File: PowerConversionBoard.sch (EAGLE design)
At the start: 31 parts, among them U1 LM2678, U2 LM2678

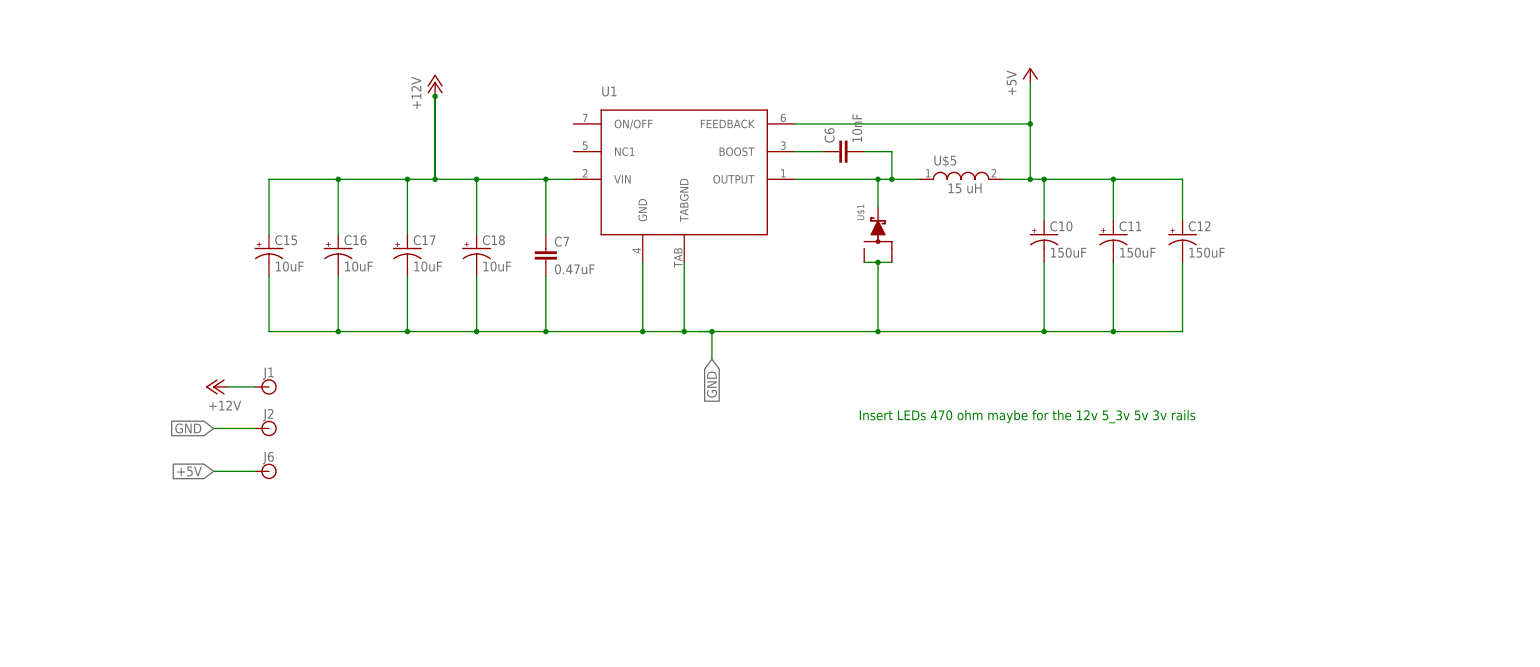
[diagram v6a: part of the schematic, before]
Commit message: Added LEDs to schematic
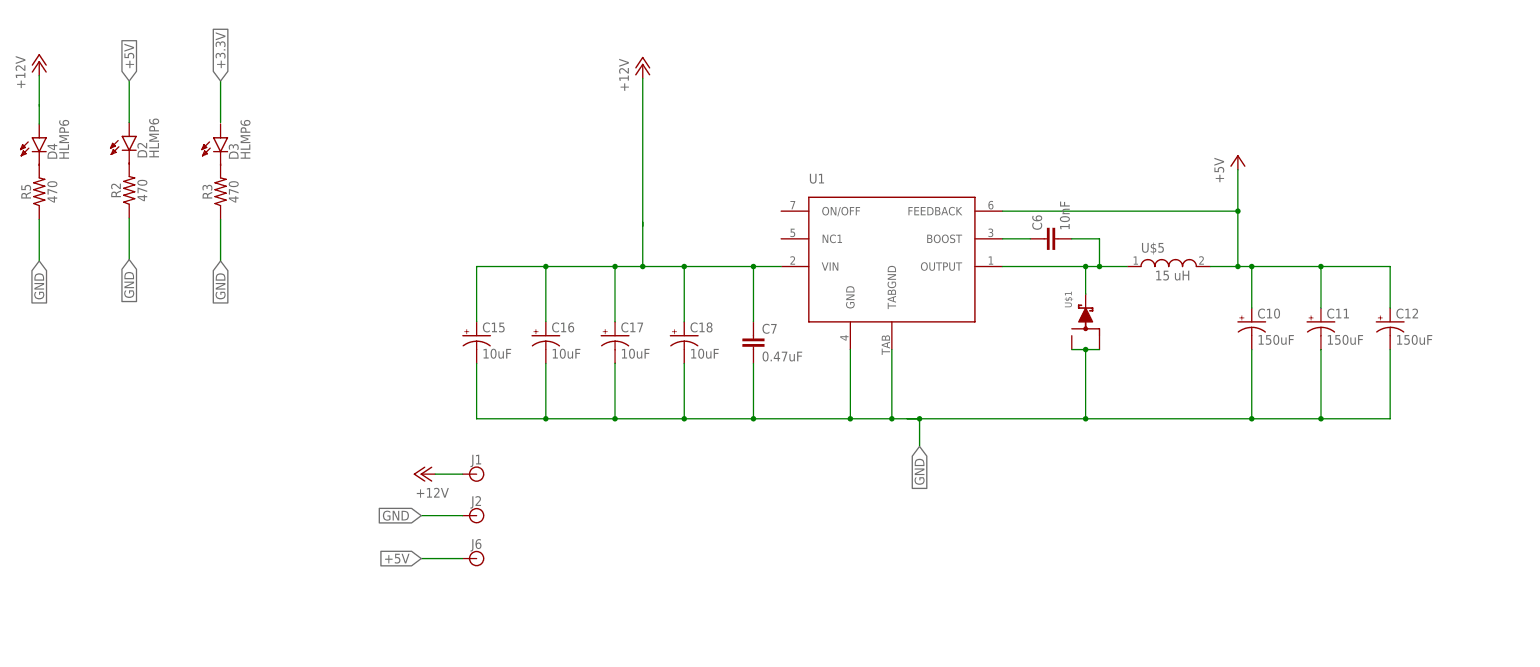
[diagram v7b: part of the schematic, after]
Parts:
- added D2, D3, D4: HLMP6, display-hp:HLMP6
- added R2, R3, R5: 470, SparkFun-Resistors:470OHM-0603-1/10W-1%
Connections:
- new net N$4: C15.+, C16.+, C17.+, C18.+, C7.1, U1.VIN
- net +12V: now also D4.A; no longer C15.+, C16.+, C17.+, C18.+, C7.1, U1.VIN
- net +5V: now also D2.A
- net GND: now also R2.1, R3.1, R5.1
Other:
- note removed: "Insert LEDs 470 ohm maybe for the 12v 5_3v 5v 3v rails"
- moved on the sheet: C10, C11, C12, C15, C16, C17, C18, C6, C7, J1, J2, J6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

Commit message: Put in good LEDs
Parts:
- removed D2, D3, D4: HLMP6, display-hp:HLMP6
- added LED1, LED2, LED3: (no value), led:LEDCHIP-LED0603
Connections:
- new net N$5: LED3.A, R3.1
- net +12V: now also R5.2; no longer D4.A
- net +3.3V: now also R3.2
- net +5V: now also R2.2; no longer D2.A
- net GND: now also LED1.C, LED2.C, LED3.C; no longer R2.1, R3.1, R5.1
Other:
- moved on the sheet: R2, R3, R5
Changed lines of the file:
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@@
 <part name="U$5" library="HCM1305" deviceset="HCM1305" device=""/>
 <part name="P+6" library="supply1" library_urn="urn:adsk.eagle:library:371" deviceset="+12V" device=""/>
+<part name="P+7" library="supply1" library_urn="urn:adsk.eagle:library:371" deviceset="+12V" device=""/>
+<part name="R5" library="SparkFun-Resistors" library_urn="urn:adsk.eagle:library:532" deviceset="470OHM" device="-0603-1/10W-1%" package3d_urn="urn:adsk.eagle:package:39650/1" value="470"/>
 <part name="R2" library="SparkFun-Resistors" library_urn="urn:adsk.eagle:library:532" deviceset="470OHM" device="-0603-1/10W-1%" package3d_urn="urn:adsk.eagle:package:39650/1" value="470"/>
-<part name="D2" library="display-hp" library_urn="urn:adsk.eagle:library:212" deviceset="HLMP6" device="" package3d_urn="urn:adsk.eagle:package:12992/1"/>
-<part name="R5" library="SparkFun-Resistors" library_urn="urn:adsk.eagle:library:532" deviceset="470OHM" device="-0603-1/10W-1%" package3d_urn="urn:adsk.eagle:package:39650/1" value="470"/>
-<part name="D4" library="display-hp" library_urn="urn:adsk.eagle:library:212" deviceset="HLMP6" device="" package3d_urn="urn:adsk.eagle:package:12992/1"/>
+<part name="LED1" library="led" library_urn="urn:adsk.eagle:library:259" deviceset="LED" device="CHIP-LED0603" package3d_urn="urn:adsk.eagle:package:15819/3"/>
+<part name="LED2" library="led" library_urn="urn:adsk.eagle:library:259" deviceset="LED" device="CHIP-LED0603" package3d_urn="urn:adsk.eagle:package:15819/3"/>
 <part name="R3" library="SparkFun-Resistors" library_urn="urn:adsk.eagle:library:532" deviceset="470OHM" device="-0603-1/10W-1%" package3d_urn="urn:adsk.eagle:package:39650/1" value="470"/>
-<part name="D3" library="display-hp" library_urn="urn:adsk.eagle:library:212" deviceset="HLMP6" device="" package3d_urn="urn:adsk.eagle:package:12992/1"/>
-<part name="P+7" library="supply1" library_urn="urn:adsk.eagle:library:371" deviceset="+12V" device=""/>
+<part name="LED3" library="led" library_urn="urn:adsk.eagle:library:259" deviceset="LED" device="CHIP-LED0603" package3d_urn="urn:adsk.eagle:package:15819/3"/>
 </parts>
 <sheets>
@@
 <attribute name="VALUE" x="-8.128" y="87.376" size="1.778" layer="96" rot="R90"/>
 </instance>
-<instance part="R2" gate="G$1" x="-99.822" y="69.342" smashed="yes" rot="R90">
-<attribute name="NAME" x="-101.346" y="69.342" size="1.778" layer="95" font="vector" rot="R90" align="bottom-center"/>
-<attribute name="VALUE" x="-98.298" y="69.342" size="1.778" layer="96" font="vector" rot="R90" align="top-center"/>
-</instance>
-<instance part="D2" gate="A" x="-99.822" y="76.708" smashed="yes">
-<attribute name="NAME" x="-96.52" y="75.184" size="1.778" layer="95" rot="R90"/>
-<attribute name="VALUE" x="-94.361" y="75.184" size="1.778" layer="96" rot="R90"/>
-</instance>
-<instance part="R5" gate="G$1" x="-116.332" y="69.088" smashed="yes" rot="R90">
-<attribute name="NAME" x="-117.856" y="69.088" size="1.778" layer="95" font="vector" rot="R90" align="bottom-center"/>
-<attribute name="VALUE" x="-114.808" y="69.088" size="1.778" layer="96" font="vector" rot="R90" align="top-center"/>
-</instance>
-<instance part="D4" gate="A" x="-116.332" y="76.454" smashed="yes">
-<attribute name="NAME" x="-113.03" y="74.93" size="1.778" layer="95" rot="R90"/>
-<attribute name="VALUE" x="-110.871" y="74.93" size="1.778" layer="96" rot="R90"/>
-</instance>
-<instance part="R3" gate="G$1" x="-83.058" y="69.088" smashed="yes" rot="R90">
-<attribute name="NAME" x="-84.582" y="69.088" size="1.778" layer="95" font="vector" rot="R90" align="bottom-center"/>
-<attribute name="VALUE" x="-81.534" y="69.088" size="1.778" layer="96" font="vector" rot="R90" align="top-center"/>
-</instance>
-<instance part="D3" gate="A" x="-83.058" y="76.454" smashed="yes">
-<attribute name="NAME" x="-79.756" y="74.93" size="1.778" layer="95" rot="R90"/>
-<attribute name="VALUE" x="-77.597" y="74.93" size="1.778" layer="96" rot="R90"/>
-</instance>
 <instance part="P+7" gate="1" x="-116.332" y="92.964" smashed="yes">
 <attribute name="VALUE" x="-118.872" y="87.884" size="1.778" layer="96" rot="R90"/>
+</instance>
+<instance part="R5" gate="G$1" x="-116.332" y="76.454" smashed="yes" rot="R90">
+<attribute name="NAME" x="-117.856" y="76.454" size="1.778" layer="95" font="vector" rot="R90" align="bottom-center"/>
+<attribute name="VALUE" x="-114.808" y="76.454" size="1.778" layer="96" font="vector" rot="R90" align="top-center"/>
+</instance>
+<instance part="R2" gate="G$1" x="-99.822" y="76.708" smashed="yes" rot="R90">
+<attribute name="NAME" x="-101.346" y="76.708" size="1.778" layer="95" font="vector" rot="R90" align="bottom-center"/>
+<attribute name="VALUE" x="-98.298" y="76.708" size="1.778" layer="96" font="vector" rot="R90" align="top-center"/>
+</instance>
+<instance part="LED1" gate="G$1" x="-116.332" y="69.088" smashed="yes">
+<attribute name="NAME" x="-112.776" y="64.516" size="1.778" layer="95" rot="R90"/>
+<attribute name="VALUE" x="-110.617" y="64.516" size="1.778" layer="96" rot="R90"/>
+</instance>
+<instance part="LED2" gate="G$1" x="-99.822" y="69.342" smashed="yes">
+<attribute name="NAME" x="-96.266" y="64.77" size="1.778" layer="95" rot="R90"/>
+<attribute name="VALUE" x="-94.107" y="64.77" size="1.778" layer="96" rot="R90"/>
+</instance>
+<instance part="R3" gate="G$1" x="291.592" y="82.042" smashed="yes" rot="R90">
+<attribute name="NAME" x="290.068" y="82.042" size="1.778" layer="95" font="vector" rot="R90" align="bottom-center"/>
+<attribute name="VALUE" x="293.116" y="82.042" size="1.778" layer="96" font="vector" rot="R90" align="top-center"/>
+</instance>
+<instance part="LED3" gate="G$1" x="291.592" y="74.422" smashed="yes">
+<attribute name="NAME" x="295.148" y="69.85" size="1.778" layer="95" rot="R90"/>
+<attribute name="VALUE" x="297.307" y="69.85" size="1.778" layer="96" rot="R90"/>
 </instance>
 </instances>
@@
 </segment>
 <segment>
-<pinref part="D4" gate="A" pin="A"/>
-<wire x1="-116.332" y1="81.534" x2="-116.332" y2="84.836" width="0.1524" layer="91"/>
 <pinref part="P+7" gate="1" pin="+12V"/>
-<wire x1="-116.332" y1="84.836" x2="-116.332" y2="85.09" width="0.1524" layer="91"/>
-<wire x1="-116.332" y1="90.424" x2="-116.332" y2="85.09" width="0.1524" layer="91"/>
+<wire x1="-116.332" y1="90.424" x2="-116.332" y2="81.534" width="0.1524" layer="91"/>
+<pinref part="R5" gate="G$1" pin="2"/>
 </segment>
 </net>
@@
 <wire x1="-99.822" y1="64.262" x2="-99.822" y2="56.642" width="0.1524" layer="91"/>
 <label x="-99.822" y="56.642" size="1.778" layer="95" rot="R270" xref="yes"/>
-<pinref part="R2" gate="G$1" pin="1"/>
+<pinref part="LED2" gate="G$1" pin="C"/>
 </segment>
 <segment>
 <wire x1="-116.332" y1="64.008" x2="-116.332" y2="56.388" width="0.1524" layer="91"/>
 <label x="-116.332" y="56.388" size="1.778" layer="95" rot="R270" xref="yes"/>
-<pinref part="R5" gate="G$1" pin="1"/>
-</segment>
-<segment>
-<wire x1="-83.058" y1="64.008" x2="-83.058" y2="56.388" width="0.1524" layer="91"/>
-<label x="-83.058" y="56.388" size="1.778" layer="95" rot="R270" xref="yes"/>
-<pinref part="R3" gate="G$1" pin="1"/>
+<pinref part="LED1" gate="G$1" pin="C"/>
+</segment>
+<segment>
+<wire x1="291.592" y1="69.342" x2="291.592" y2="61.722" width="0.1524" layer="91"/>
+<label x="291.592" y="61.722" size="1.778" layer="95" rot="R270" xref="yes"/>
+<pinref part="LED3" gate="G$1" pin="C"/>
 </segment>
 </net>
@@
 <wire x1="-99.822" y1="81.788" x2="-99.822" y2="89.408" width="0.1524" layer="91"/>
 <label x="-99.822" y="89.408" size="1.778" layer="95" rot="R90" xref="yes"/>
-<pinref part="D2" gate="A" pin="A"/>
+<pinref part="R2" gate="G$1" pin="2"/>
 </segment>
 </net>
@@
 </segment>
 <segment>
-<wire x1="-83.058" y1="81.788" x2="-83.058" y2="89.408" width="0.1524" layer="91"/>
-<label x="-83.058" y="89.408" size="1.778" layer="95" rot="R90" xref="yes"/>
+<wire x1="291.592" y1="87.122" x2="291.592" y2="94.742" width="0.1524" layer="91"/>
+<label x="291.592" y="94.742" size="1.778" layer="95" rot="R90" xref="yes"/>
+<pinref part="R3" gate="G$1" pin="2"/>
 </segment>
 </net>
@@
 </segment>
 </net>
+<net name="N$5" class="0">
+<segment>
+<pinref part="LED3" gate="G$1" pin="A"/>
+<pinref part="R3" gate="G$1" pin="1"/>
+</segment>
+</net>
